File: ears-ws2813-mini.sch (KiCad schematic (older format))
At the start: 75 parts, among them J1 Conn_01x08

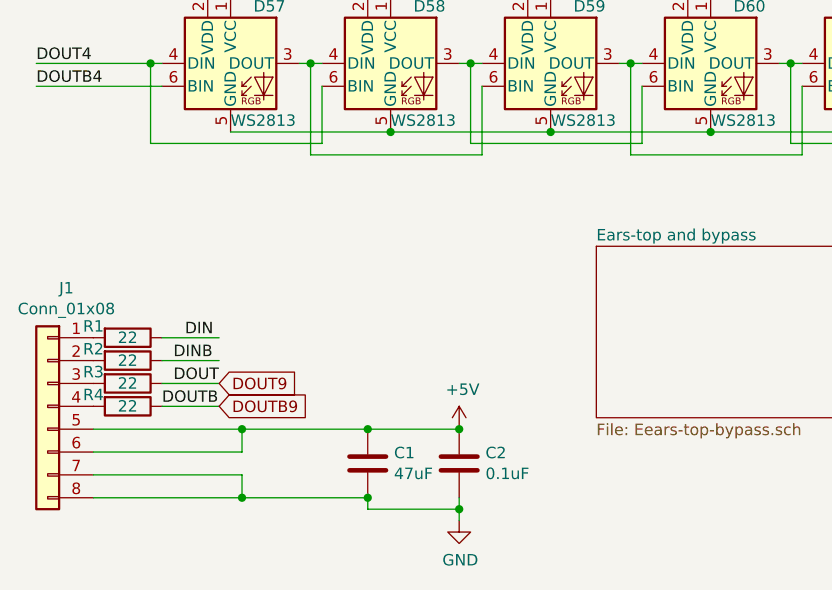
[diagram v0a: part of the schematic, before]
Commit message: Cleaned up ears and added protection diode.
The diode should short things out should power and ground be
reversed.

Added new footprint for WS2813B-Minis.  Note that this footprint has
not yet been tested.

Signed-off-by: aaronw <aaron.w2@gmail.com>
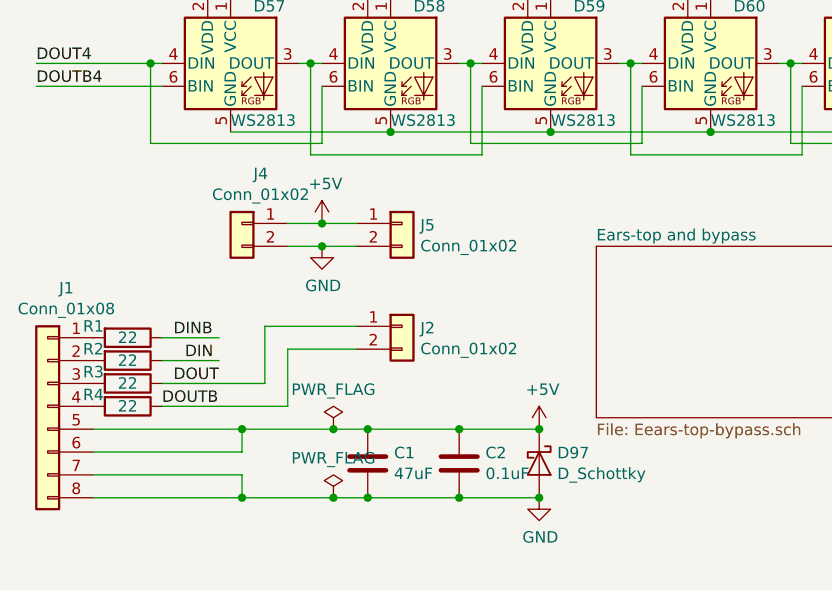
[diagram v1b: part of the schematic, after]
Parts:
- added D97: D_Schottky, Diode_SMD:D_2010_5025Metric, symbol Device:D_Schottky
- added J2, J4, J5: Conn_01x02, Connector_PinHeader_2.54mm:PinHeader_1x02_P2.54mm_Vertical, symbol Connector_Generic:Conn_01x02
- C1, R1, R2, R3, R4: MFR (none) -> -; MPN (none) -> -; SPN (none) -> -; SPR (none) -> -; SPURL (none) -> -
- C2: MFR (none) -> Samsung; MPN (none) -> CL10B104KO8WPNC; SPN (none) -> 1276-6582-1-ND; SPR (none) -> Digikey; SPURL (none) -> -
- D1, D10, D11, D12, D13, D14, D15, D16, D17, D18, D19, D2, D20, D21, D22, D23, D24, D25, D26, D27, D28, D29, D3, D30, D31, D32, D33, D34, D35, D36, D37, D38, D39, D4, D40, D41, D42, D43, D44, D45, D46, D47, D48, D49, D5, D50, D51, D52, D53, D54, D55, D56, D57, D58, D59, D6, D60, D61, D62, D63, D64, D65, D66, D67, D68, D7, D8, D9: MFR (none) -> World Semi; MPN (none) -> WS2813B-Mini; SPN (none) -> -; SPR (none) -> -; SPURL (none) -> -
- J1: footprint (none) -> Connector_PinHeader_2.54mm:PinHeader_1x08_P2.54mm_Vertical; MFR (none) -> -; MPN (none) -> -; SPN (none) -> -; SPR (none) -> -; SPURL (none) -> -
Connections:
- net labels removed: DOUT9, DOUTB9
- wire segments 561 -> 570

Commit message: Hopefully this will be revision 2.0
Signed-off-by: Aaron Williams <aaron.w2@gmail.com>
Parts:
- added C100, C99: 4.7nF, Capacitor_SMD:C_0603_1608Metric, symbol Device:C
- added C101, C102: 4.7nF DNI, Capacitor_SMD:C_0603_1608Metric, symbol Device:C
- D1, D10, D11, D12, D13, D14, D15, D16, D17, D18, D19, D2, D20, D21, D22, D23, D24, D25, D26, D27, D28, D29, D3, D30, D31, D32, D33, D34, D35, D36, D37, D38, D39, D4, D40, D41, D42, D43, D44, D45, D46, D47, D48, D49, D5, D50, D51, D52, D53, D54, D55, D56, D57, D58, D59, D6, D60, D61, D62, D63, D64, D65, D66, D67, D68, D7, D8, D9: footprint LED_WS2813-mini:LED_WS2813-MINI -> LED_WS2813-mini:LED_WS2813-MINI-2
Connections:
- wire segments 570 -> 583
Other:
- moved on the sheet: C1, C2, D97, J2, R1, R2, R3, R4

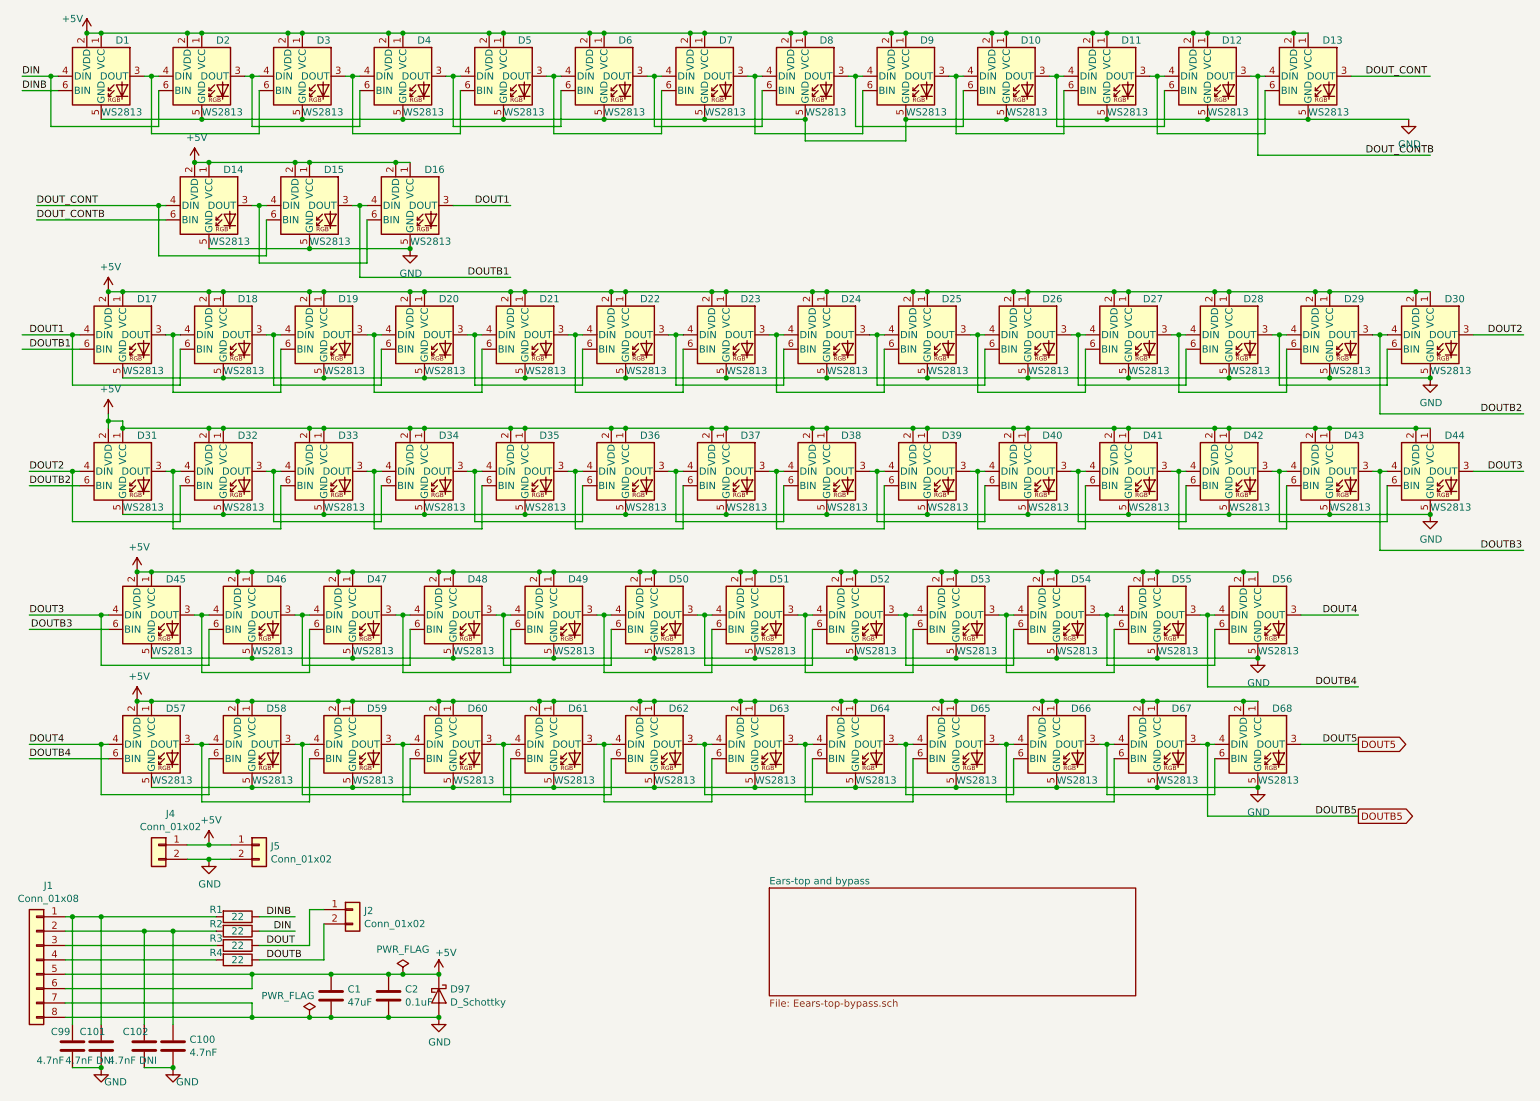
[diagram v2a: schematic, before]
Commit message: Added more ESD protection and moved a few components.
Version 2.0

Signed-off-by: Aaron Williams <aaron.w2@gmail.com>
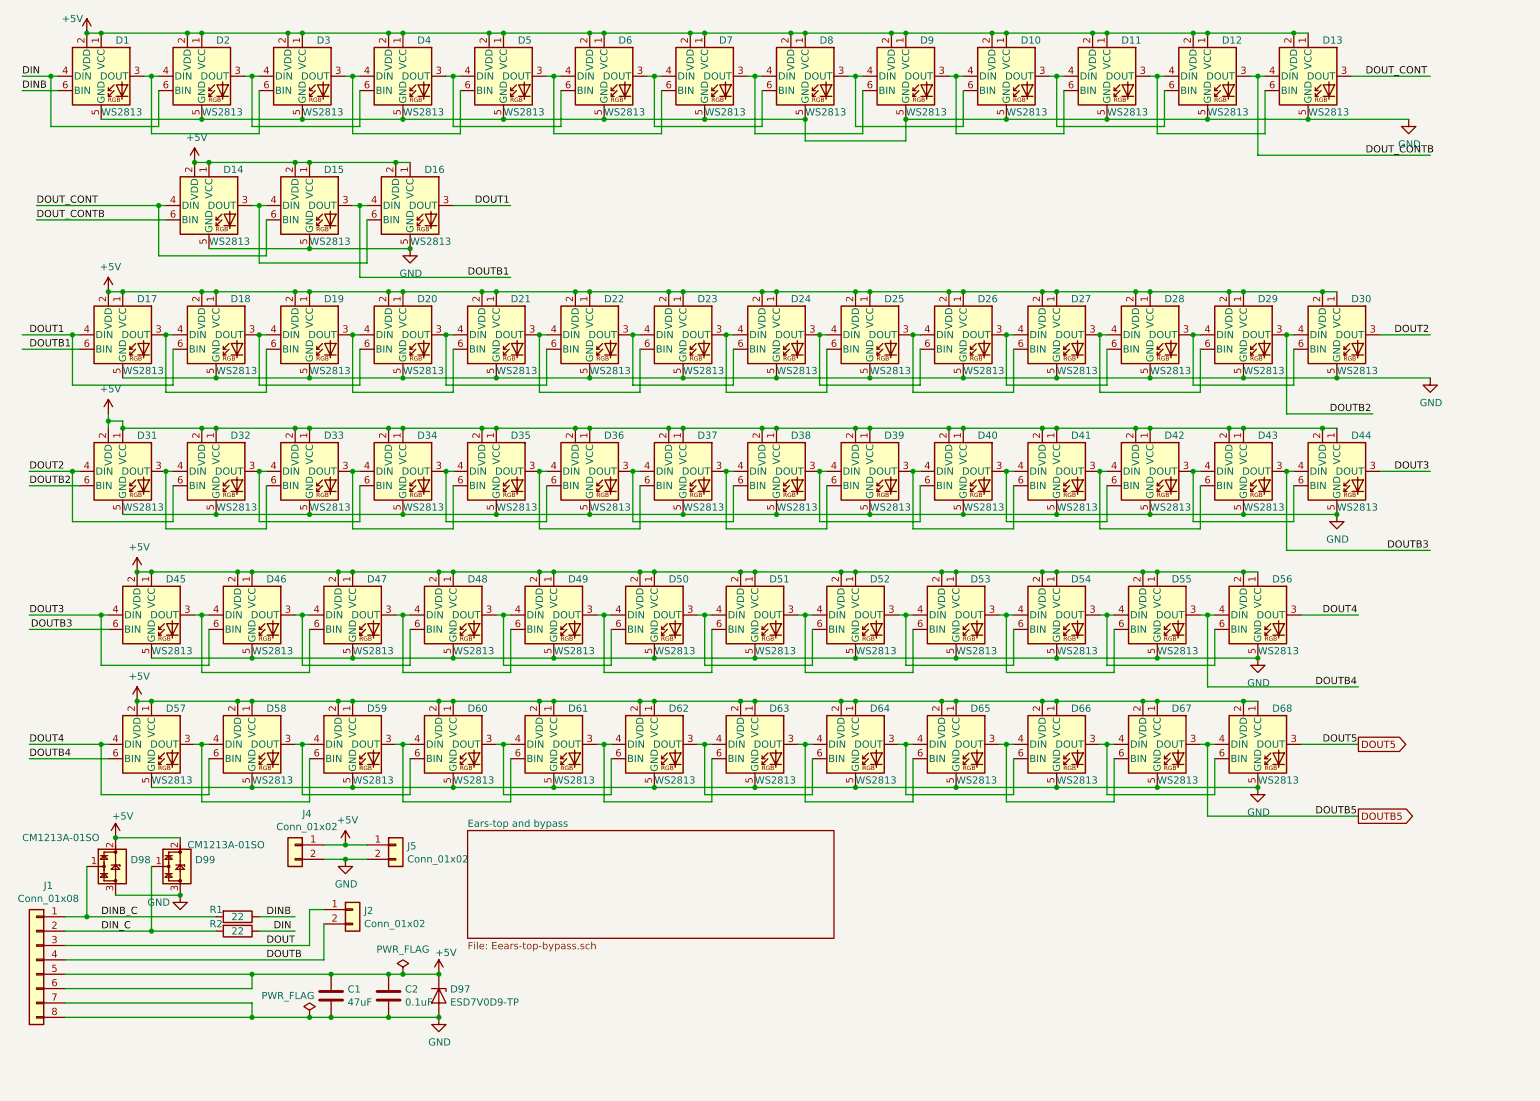
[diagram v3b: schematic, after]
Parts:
- removed C100, C99: 4.7nF, Capacitor_SMD:C_0603_1608Metric, symbol Device:C
- removed C101, C102: 4.7nF DNI, Capacitor_SMD:C_0603_1608Metric, symbol Device:C
- removed D97: D_Schottky, Diode_SMD:D_2010_5025Metric, symbol Device:D_Schottky
- removed R3, R4: 22, Resistor_SMD:R_0603_1608Metric, symbol Device:R
- added D97: ESD7V0D9-TP, Diode_SMD:D_SOD-932, symbol Aaron:ESD7V0D9-TP
- added D98, D99: CM1213A-01SO, Package_TO_SOT_SMD:SOT-23, symbol Power_Protection:CM1213A-01SO
- C1: MFR - -> Murata Electronics; MPN - -> GCJ32ER70J476KE01L; SPN - -> 490-10559-1-ND; SPR - -> Digikey
- R1, R2: MFR - -> Yageo; MPN - -> AC0603FR-0722RL; SPN - -> YAG3581CT-ND; SPR - -> Digikey
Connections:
- net labels added: DINB_C, DIN_C
- wire segments 583 -> 552
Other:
- moved on the sheet: D18, D19, D20, D21, D22, D23, D24, D25, D26, D27, D28, D29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
